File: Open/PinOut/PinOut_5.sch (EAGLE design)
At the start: 8 parts

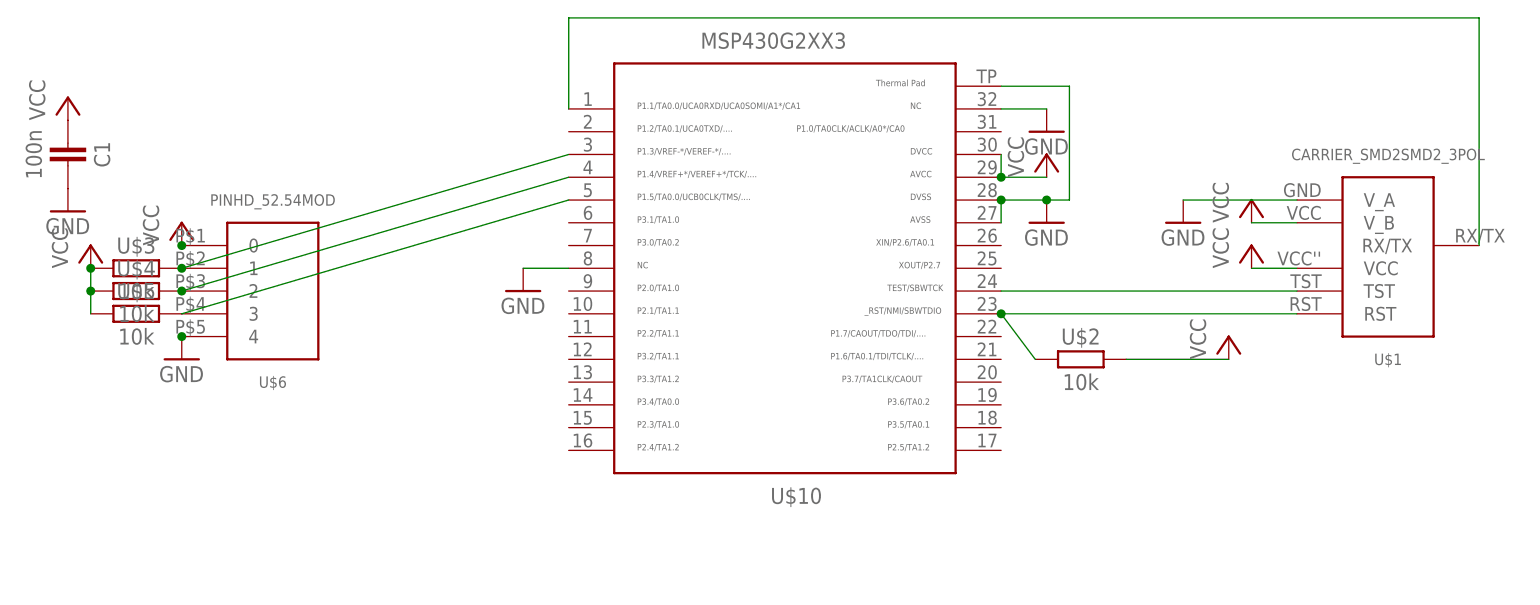
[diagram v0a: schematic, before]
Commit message: Update Pinheader
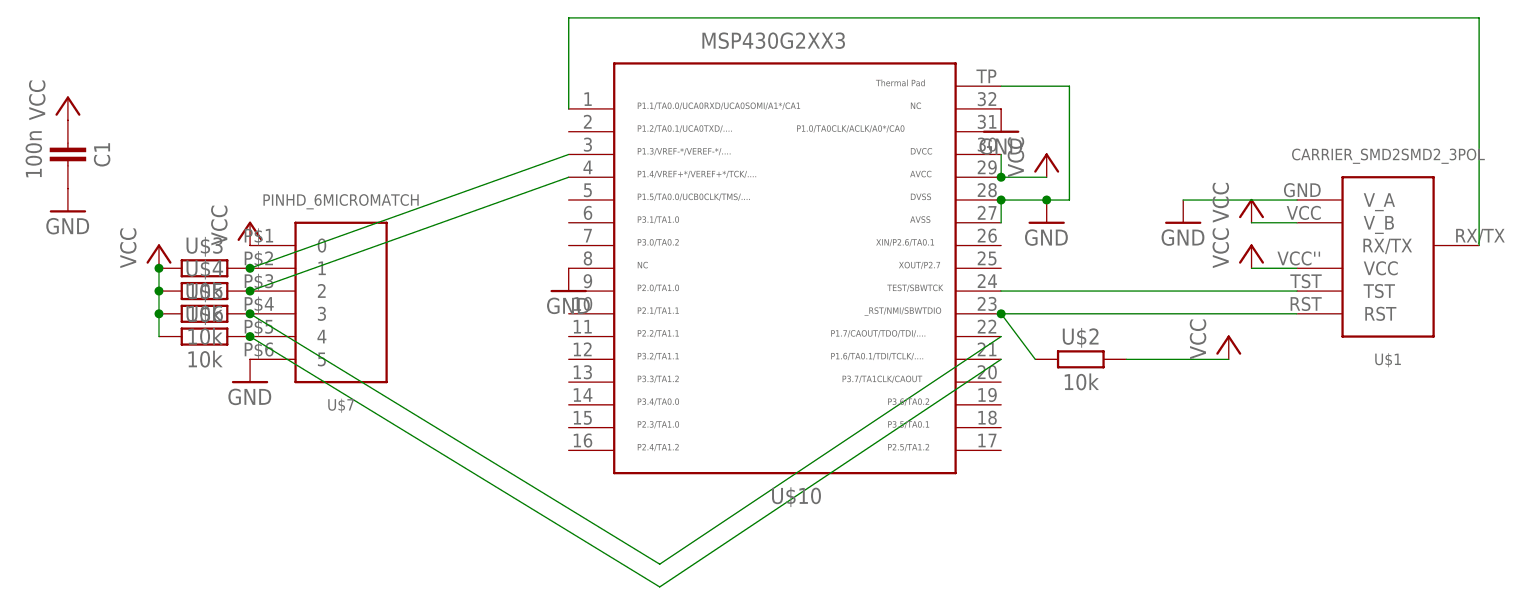
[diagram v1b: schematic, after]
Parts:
- added U$7: PINHD_6MICROMATCH, thar:PINHD_6MICROMATCH
- U$3, U$4, U$5: device thar:RESISTOR1206 -> thar:RESISTOR0603
- U$6: value PINHD_52.54MOD -> 10k; device thar:PINHD_52.54MOD -> thar:RESISTOR0603
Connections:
- new net N$7: U$10.3, U$3.2, U$7.1
- net GND: now also U$7.5; no longer U$6.4
- net N$2: now also U$10.22, U$5.2, U$7.3; no longer U$10.3, U$3.2, U$6.1
- net N$5: now also U$10.21, U$7.4; no longer U$10.4, U$4.2
- net N$6: now also U$10.4, U$4.2, U$7.2; no longer U$10.5, U$5.2, U$6.3
- net VCC: now also U$6.1, U$7.0; no longer U$6.0
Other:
- moved on the sheet: U$3, U$4, U$5
